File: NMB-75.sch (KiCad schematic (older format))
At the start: 24 parts

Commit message: footprints assigned
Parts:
- C1, C2, C3, C4, C5, C6, C7: renamed from C?; footprint (none) -> Capacitor_SMD:C_0805_2012Metric
- D1, D2, D3, D4: renamed from D?; footprint (none) -> Diode_SMD:D_SOD-123
- F1: renamed from F?; footprint (none) -> Fuse:Fuse_1206_3216Metric
- MX1, MX2, MX3, MX4: renamed from MX?; footprint (none) -> MX_Alps_Hybrid:MX-1U-NoLED
- R1, R2, R3, R4: renamed from R?; footprint (none) -> Resistor_SMD:R_1206_3216Metric
- SW1: renamed from SW?; footprint (none) -> random-keyboard-parts:SKQG-1155865
- USB1: renamed from USB?; footprint (none) -> random-keyboard-parts:Molex-0548190589
- Y1: renamed from Y?; footprint (none) -> Crystal:Crystal_SMD_3225-4Pin_3.2x2.5mm
- gave numbers to parts that had none: 1

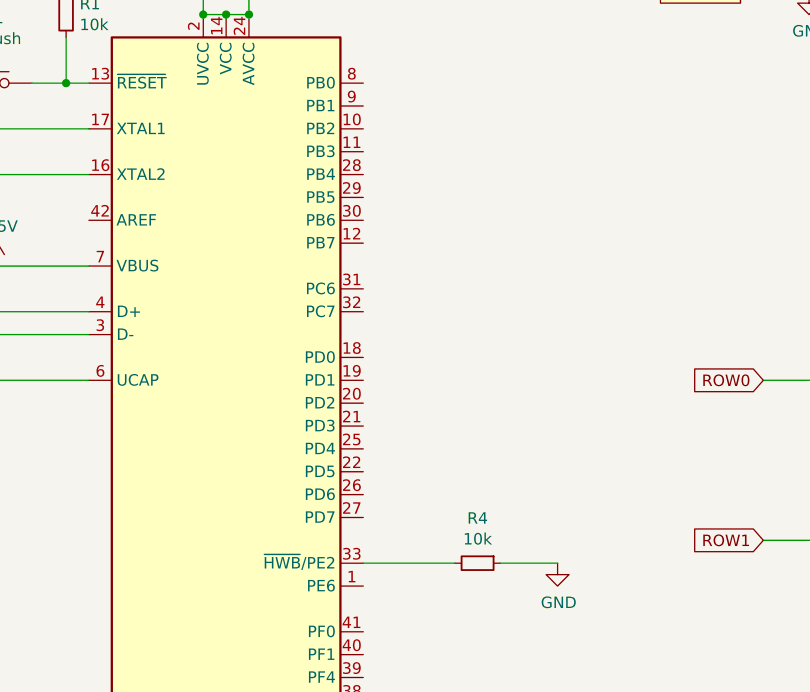
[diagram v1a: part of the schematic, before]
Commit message: routing finished on learning board
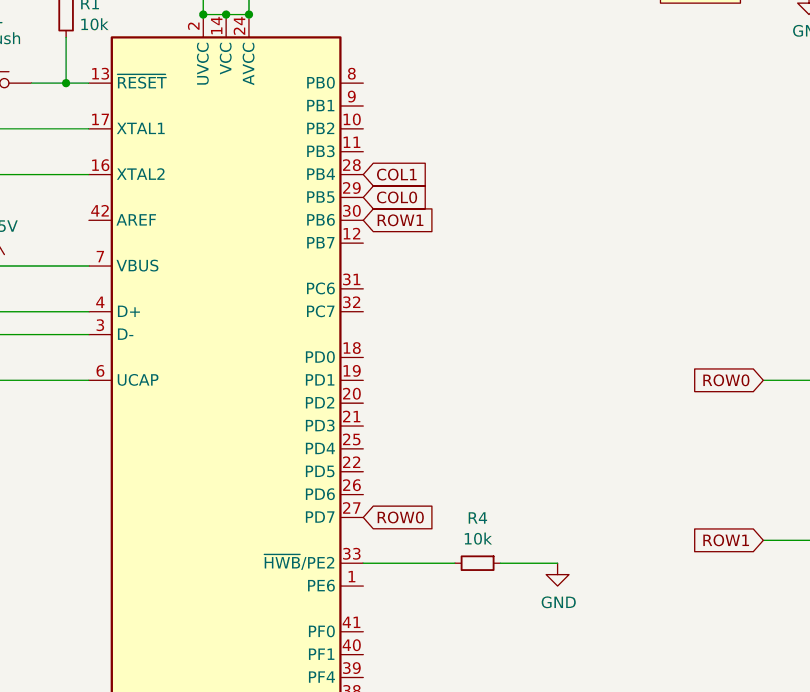
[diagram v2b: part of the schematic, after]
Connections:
- net COL0: now also U1.29 (PB5)
- net COL1: now also U1.28 (PB4)
- net ROW0: now also U1.27 (PD7)
- net ROW1: now also U1.30 (PB6)
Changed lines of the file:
@@
 EESchema Schematic File Version 4
+LIBS:NMB-75-cache
 EELAYER 30 0
 EELAYER END
@@
 	3300 6000 3300 6300
 Connection ~ 3300 6000
+Text GLabel 3900 3100 2    50   Input ~ 0
+COL1
+Text GLabel 3900 3200 2    50   Input ~ 0
+COL0
+Text GLabel 3900 3300 2    50   Input ~ 0
+ROW1
+Text GLabel 3900 4600 2    50   Input ~ 0
+ROW0
 $EndSCHEMATC
